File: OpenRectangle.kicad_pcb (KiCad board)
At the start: 2 copper layers, 339.1 x 141.2 mm, 84 parts, among them J1 USB C Connector, J2 JTAG_TC2030, SW1 MX_SW_HS, SW10 MX_SW_HS, SW11 MX_SW_HS, SW12 MX_SW_solder, SW13 MX_SW_HS, SW14 MX_SW_solder, SW15 MX_SW_solder, SW16 MX_SW_HS, SW17 MX_SW_HS, SW18 MX_SW_solder, SW19 MX_SW_HS, SW2 MX_SW_solder, SW20 MX_SW_solder, SW21 MX_SW_solder, SW22 MX_SW_HS, SW23 MX_SW_HS, SW24 MX_SW_solder, SW25 MX_SW_solder, SW26 MX_SW_HS, SW27 MX_SW_solder, SW28 MX_SW_HS, SW29 MX_SW_HS, SW3 MX_SW_HS, SW30 MX_SW_solder, SW31 MX_SW_solder, SW32 MX_SW_HS, SW33 MX_SW_solder, SW34 MX_SW_HS, SW35 MX_SW_HS, SW36 MX_SW_solder, SW37 MX_SW_solder, SW38 MX_SW_HS, SW39 MX_SW_HS, SW4 MX_SW_solder, SW40 MX_SW_solder, SW41 Boot, SW5 MX_SW_HS, SW6 MX_SW_solder, SW7 MX_SW_HS, SW8 MX_SW_solder, SW9 MX_SW_solder, U1 XC6206, U2 USBLC6-2SC6, U3 RP2040, U4 W25Q128JVS, Y1 12MHz

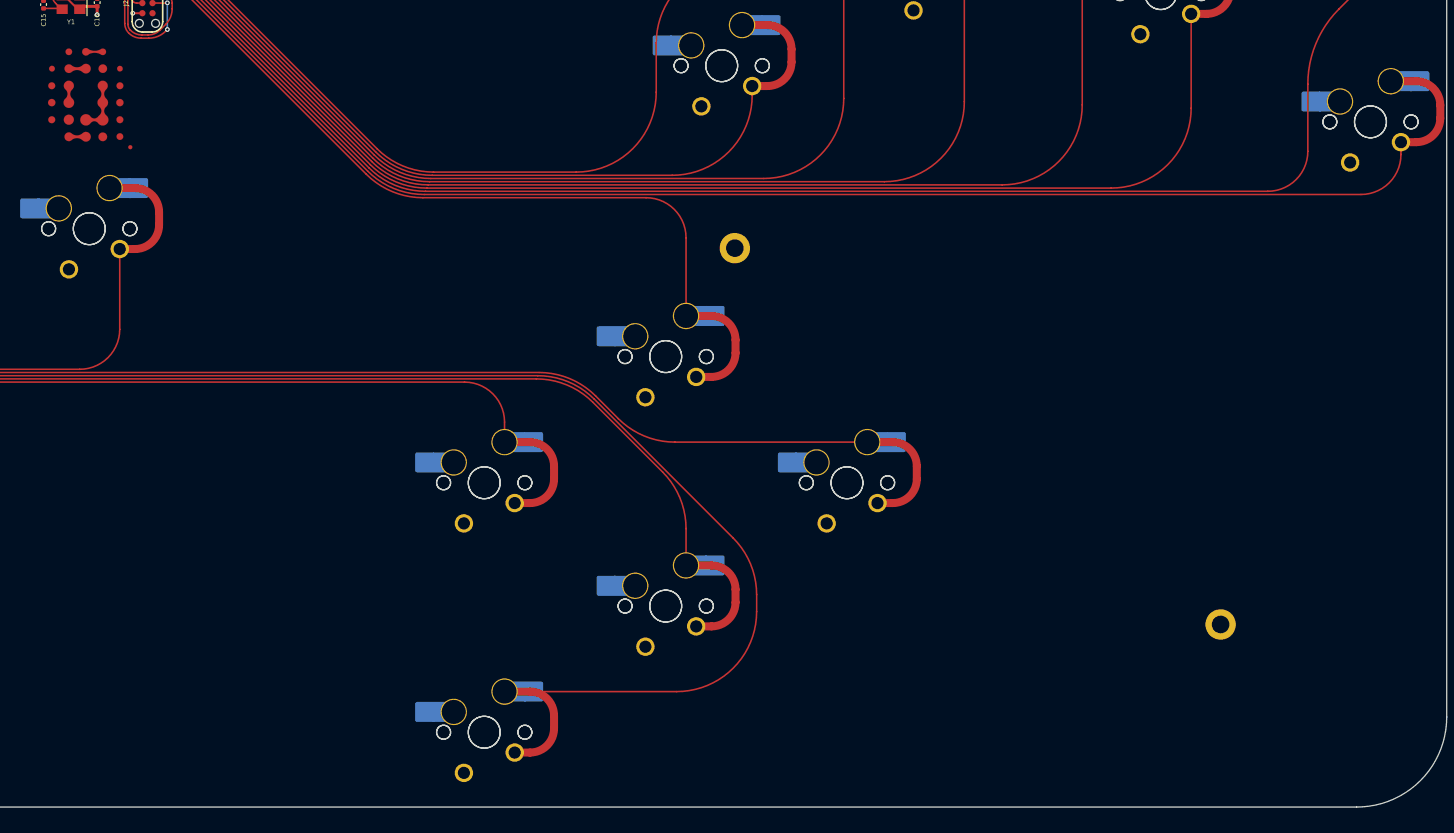
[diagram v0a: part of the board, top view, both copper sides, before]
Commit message: Added case to the old paneled version
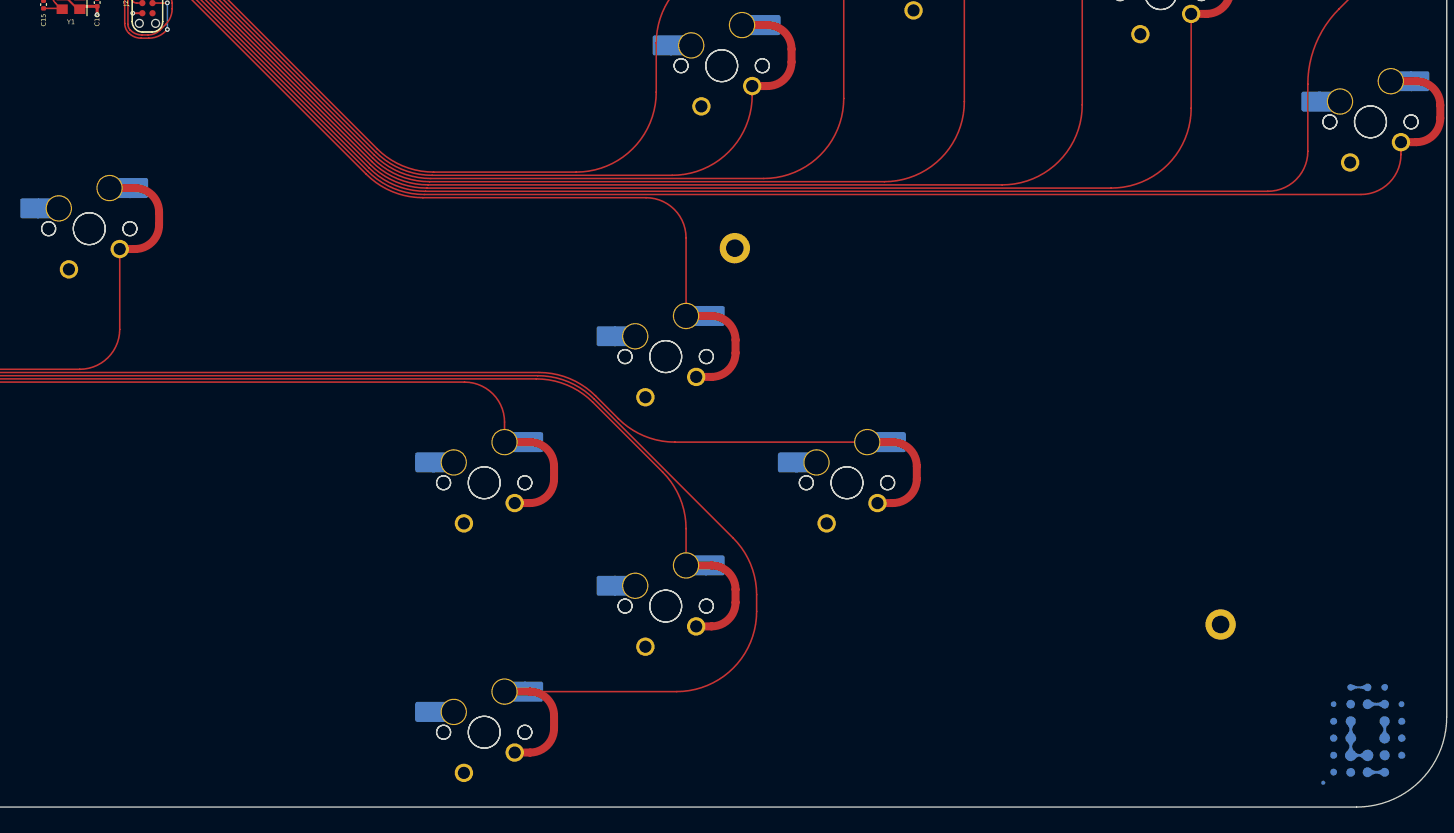
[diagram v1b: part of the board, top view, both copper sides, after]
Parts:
- added G***: LOGO, LOGO, B.Cu at (199.9, 96.4)
- H11: moved to B.Cu
- moved H11 177.9 mm to (357.8, 157.5), turned to 180 degrees
